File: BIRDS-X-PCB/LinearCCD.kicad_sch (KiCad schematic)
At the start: 11 parts, among them IC601 TCD1103GFG_8Z,AA2_, Q601 2SA1015, U601 74HC04

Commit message: Layout and route a bit
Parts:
- R601, R602, R603: footprint (none) -> Resistor_SMD:R_0603_1608Metric_Pad0.98x0.95mm_HandSolder
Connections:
- net PHI_M_INPUT: now also U601.5; no longer U601.1
- net PHI_M_PIN: now also U601.6; no longer U601.2
- net SH_INPUT: now also U601.1; no longer U601.5
- net SH_PIN: now also U601.2; no longer U601.6
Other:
- moved on the sheet: U601A, U601C
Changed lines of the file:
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@@
     (effects (font (size 1.27 1.27)) (justify right))
   )
-  (symbol (lib_id "74xx:74HC04") (at 83.82 97.79 0) (unit 3)
-    (in_bom yes) (on_board yes) (dnp no) (fields_autoplaced)
-    (property "Reference" "U601" (at 83.82 88.9 0)
-      (effects (font (size 1.27 1.27)))
-    )
-    (property "Value" "74HC04" (at 83.82 91.44 0)
-      (effects (font (size 1.27 1.27)))
-    )
-    (property "Footprint" "Package_SO:SOIC-14_3.9x8.7mm_P1.27mm" (at 83.82 97.79 0)
-      (effects (font (size 1.27 1.27)) hide)
-    )
-    (property "Datasheet" "https://assets.nexperia.com/documents/data-sheet/74HC_HCT04.pdf" (at 83.82 97.79 0)
-      (effects (font (size 1.27 1.27)) hide)
-    )
-    (property "LCSC" "C86613" (at 83.82 97.79 0)
+  (symbol (lib_id "74xx:74HC04") (at 83.82 68.58 0) (unit 3)
+    (in_bom yes) (on_board yes) (dnp no) (fields_autoplaced)
+    (property "Reference" "U601" (at 83.82 59.69 0)
+      (effects (font (size 1.27 1.27)))
+    )
+    (property "Value" "74HC04" (at 83.82 62.23 0)
+      (effects (font (size 1.27 1.27)))
+    )
+    (property "Footprint" "Package_SO:SOIC-14_3.9x8.7mm_P1.27mm" (at 83.82 68.58 0)
+      (effects (font (size 1.27 1.27)) hide)
+    )
+    (property "Datasheet" "https://assets.nexperia.com/documents/data-sheet/74HC_HCT04.pdf" (at 83.82 68.58 0)
+      (effects (font (size 1.27 1.27)) hide)
+    )
+    (property "LCSC" "C86613" (at 83.82 68.58 0)
       (effects (font (size 1.27 1.27)) hide)
     )
@@
       (effects (font (size 1.27 1.27)) (justify right))
     )
-    (property "Footprint" "" (at 234.188 69.85 90)
+    (property "Footprint" "Resistor_SMD:R_0603_1608Metric_Pad0.98x0.95mm_HandSolder" (at 234.188 69.85 90)
       (effects (font (size 1.27 1.27)) hide)
     )
@@
       (effects (font (size 1.27 1.27)))
     )
-    (property "Footprint" "" (at 215.9 85.598 90)
+    (property "Footprint" "Resistor_SMD:R_0603_1608Metric_Pad0.98x0.95mm_HandSolder" (at 215.9 85.598 90)
       (effects (font (size 1.27 1.27)) hide)
     )
@@
     )
   )
-  (symbol (lib_id "74xx:74HC04") (at 83.82 68.58 0) (unit 1)
-    (in_bom yes) (on_board yes) (dnp no) (fields_autoplaced)
-    (property "Reference" "U601" (at 83.82 59.69 0)
-      (effects (font (size 1.27 1.27)))
-    )
-    (property "Value" "74HC04" (at 83.82 62.23 0)
-      (effects (font (size 1.27 1.27)))
-    )
-    (property "Footprint" "Package_SO:SOIC-14_3.9x8.7mm_P1.27mm" (at 83.82 68.58 0)
-      (effects (font (size 1.27 1.27)) hide)
-    )
-    (property "Datasheet" "https://assets.nexperia.com/documents/data-sheet/74HC_HCT04.pdf" (at 83.82 68.58 0)
-      (effects (font (size 1.27 1.27)) hide)
-    )
-    (property "LCSC" "C86613" (at 83.82 68.58 0)
+  (symbol (lib_id "74xx:74HC04") (at 83.82 97.79 0) (unit 1)
+    (in_bom yes) (on_board yes) (dnp no) (fields_autoplaced)
+    (property "Reference" "U601" (at 83.82 88.9 0)
+      (effects (font (size 1.27 1.27)))
+    )
+    (property "Value" "74HC04" (at 83.82 91.44 0)
+      (effects (font (size 1.27 1.27)))
+    )
+    (property "Footprint" "Package_SO:SOIC-14_3.9x8.7mm_P1.27mm" (at 83.82 97.79 0)
+      (effects (font (size 1.27 1.27)) hide)
+    )
+    (property "Datasheet" "https://assets.nexperia.com/documents/data-sheet/74HC_HCT04.pdf" (at 83.82 97.79 0)
+      (effects (font (size 1.27 1.27)) hide)
+    )
+    (property "LCSC" "C86613" (at 83.82 97.79 0)
       (effects (font (size 1.27 1.27)) hide)
     )
@@
       (effects (font (size 1.27 1.27)) (justify left))
     )
-    (property "Footprint" "" (at 230.632 97.79 90)
-      (effects (font (size 1.27 1.27)) hide)
-    )
+    (property "Footprint" "Resistor_SMD:R_0603_1608Metric_Pad0.98x0.95mm_HandSolder" (at 230.632 97.79 90)
+      (effects (font (size 1.27 1.27)) hide)
+    )

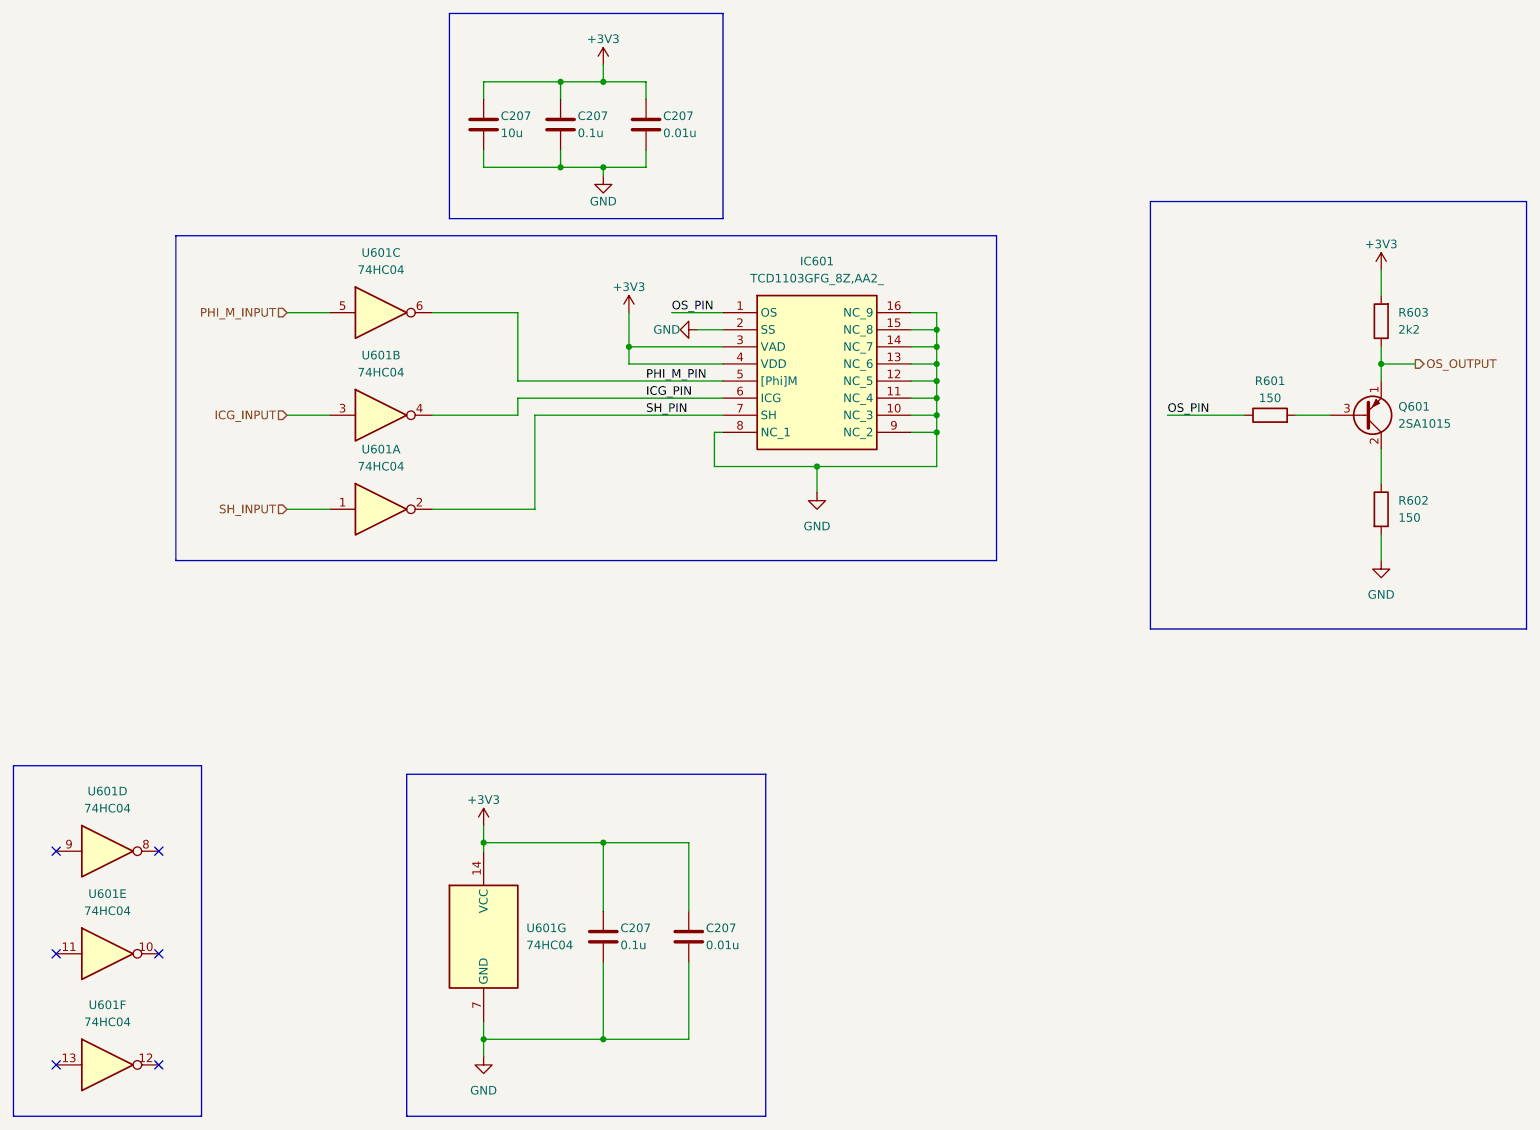
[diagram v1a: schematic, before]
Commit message: Schematic re-work (esp. RADFET fixes)
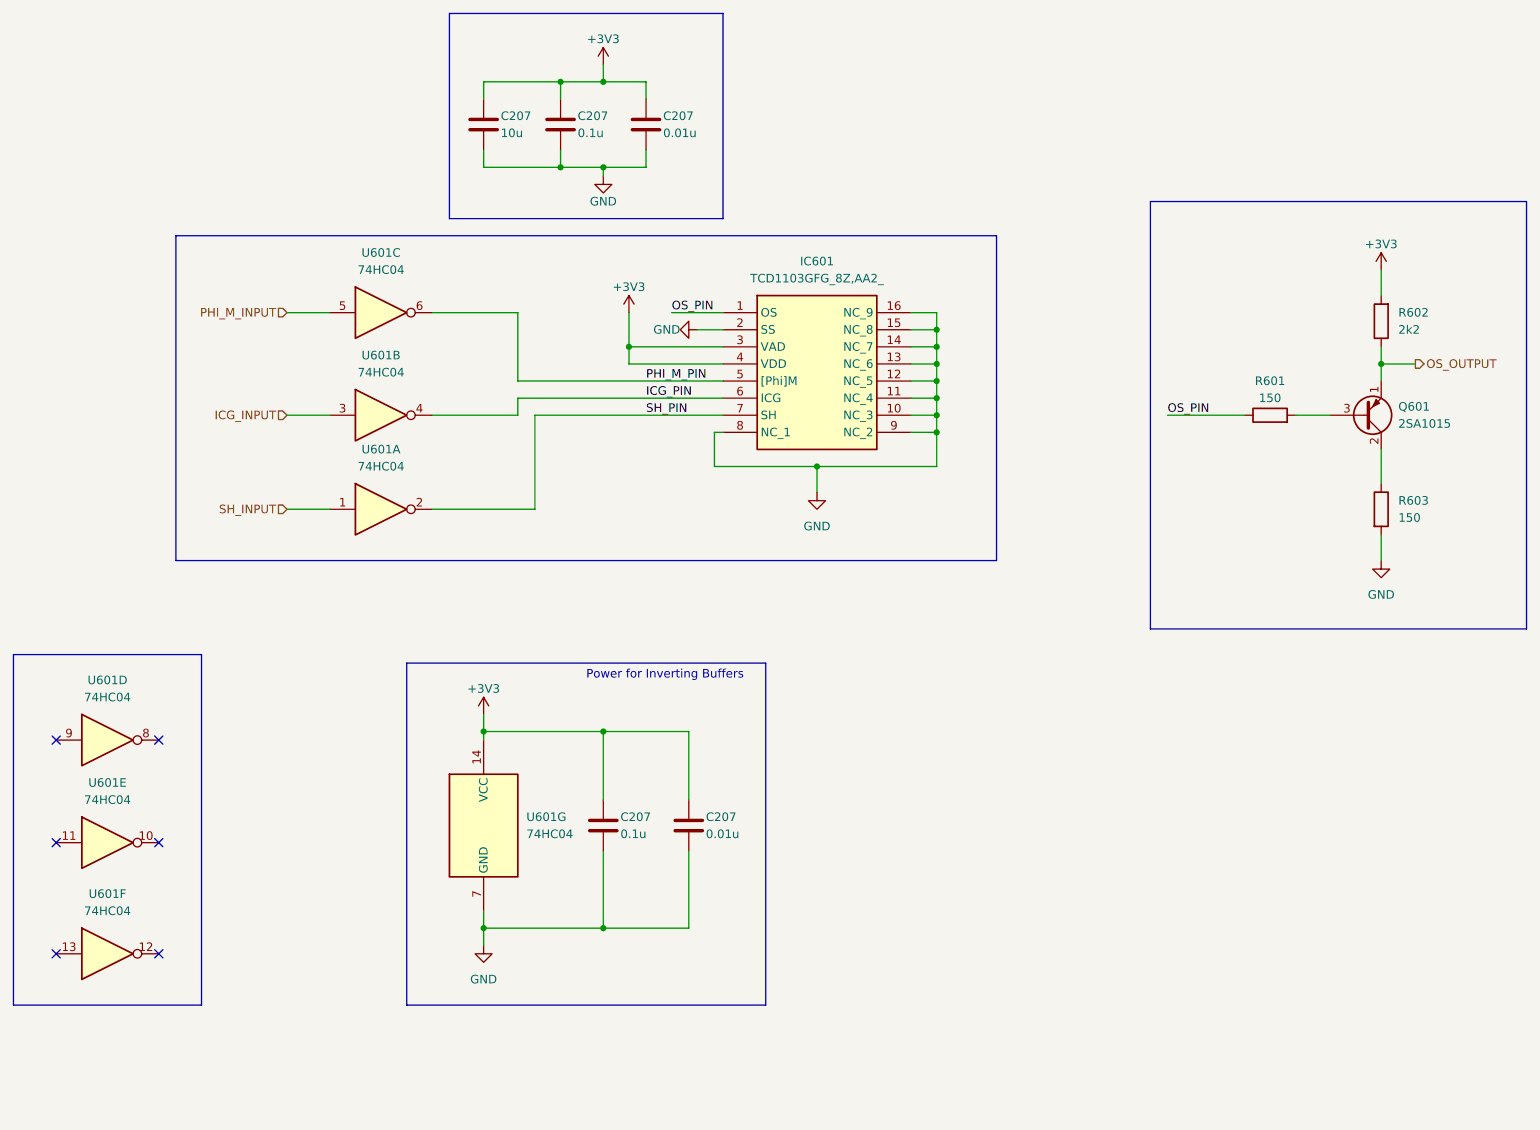
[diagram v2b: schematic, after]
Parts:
- renumbered R603 to R602, R602 to R603
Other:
- note added: "Power for Inverting Buffers"
- moved on the sheet: C207, U601D, U601E, U601F, U601G

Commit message: Fix BJT on CCD circuit
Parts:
- removed Q601: 2SA1015, Package_TO_SOT_THT:TO-92_Inline, symbol Transistor_BJT:2SA1015
- added Q601: 2SA1015, Package_TO_SOT_SMD:SOT-23, symbol BIRDS-X_Symbols_Lib:2SA1015_SMT
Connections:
- net OS_OUTPUT: now also Q601.2 (E)
- net at R601.2: now also Q601.1 (B)
- net at R603.1: now also Q601.3 (C)
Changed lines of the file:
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@@
+    )
+  )
+  (symbol (lib_id "BIRDS-X_Symbols_Lib:2SA1015_SMT") (at 229.87 83.82 0) (mirror x) (unit 1)
+    (in_bom yes) (on_board yes) (dnp no) (fields_autoplaced)
+    (property "Reference" "Q601" (at 234.95 82.55 0)
+      (effects (font (size 1.27 1.27)) (justify left))
+    )
+    (property "Value" "2SA1015" (at 234.95 85.09 0)
+      (effects (font (size 1.27 1.27)) (justify left))
+    )
+    (property "Footprint" "Package_TO_SOT_SMD:SOT-23" (at 233.68 68.58 0)
+      (effects (font (size 1.27 1.27) italic) (justify left) hide)
+    )
+    (property "Datasheet" "https://datasheet.lcsc.com/lcsc/2210101800_HXY-MOSFET-2SA1015_C5189099.pdf" (at 228.6 64.77 0)
+      (effects (font (size 1.27 1.27)) (justify left) hide)
+    )
+    (property "Datasheet_Orig" "http://www.datasheetcatalog.org/datasheet/toshiba/905.pdf" (at 257.81 60.96 0)
+      (effects (font (size 1.27 1.27)) hide)
+    )
+    (property "LCSC" "C5189099" (at 229.87 83.82 0)
+      (effects (font (size 1.27 1.27)) hide)
+    )
+    (pin "1")
+    (pin "3")
+    (pin "2")
+    (instances
+      (project "BIRDS-X-PCB"
+        (path "/c2796b15-795a-4d6e-ad4b-0ba87ded4bc9/6deb3b18-f0e5-4901-b4a2-9c2efdb4b3d1"
+          (reference "Q601") (unit 1)
+        )
+        (path "/c2796b15-795a-4d6e-ad4b-0ba87ded4bc9/a6fc61cf-80e2-4390-ad53-8772a39289cc"
+          (reference "Q701") (unit 1)
+        )
+      )
     )
   )
@@
         )
       )
-    )
-  )
-  (symbol (lib_id "Transistor_BJT:2SA1015") (at 229.87 83.82 0) (mirror x) (unit 1)
-    (in_bom yes) (on_board yes) (dnp no) (fields_autoplaced)
-    (property "Reference" "Q601" (at 234.95 82.55 0)
-      (effects (font (size 1.27 1.27)) (justify left))
-    )
-    (property "Value" "2SA1015" (at 234.95 85.09 0)
-      (effects (font (size 1.27 1.27)) (justify left))
-    )
-    (property "Footprint" "Package_TO_SOT_THT:TO-92_Inline" (at 234.95 81.915 0)
-      (effects (font (size 1.27 1.27) italic) (justify left) hide)
-    )
-    (property "Datasheet" "http://www.datasheetcatalog.org/datasheet/toshiba/905.pdf" (at 229.87 83.82 0)
-      (effects (font (size 1.27 1.27)) (justify left) hide)
-    )
-    (pin "2")
-    (pin "3")
-    (pin "1")
-    (instances
-      (project "BIRDS-X-PCB"
-        (path "/c2796b15-795a-4d6e-ad4b-0ba87ded4bc9/6deb3b18-f0e5-4901-b4a2-9c2efdb4b3d1"
-          (reference "Q601") (unit 1)
-        )
-        (path "/c2796b15-795a-4d6e-ad4b-0ba87ded4bc9/a6fc61cf-80e2-4390-ad53-8772a39289cc"
-          (reference "Q701") (unit 1)
-        )
-      )
